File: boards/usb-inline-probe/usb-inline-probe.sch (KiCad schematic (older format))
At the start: 8 parts, among them J1 USB_B, J2 USB_A, J3 SMA, J4 SMA

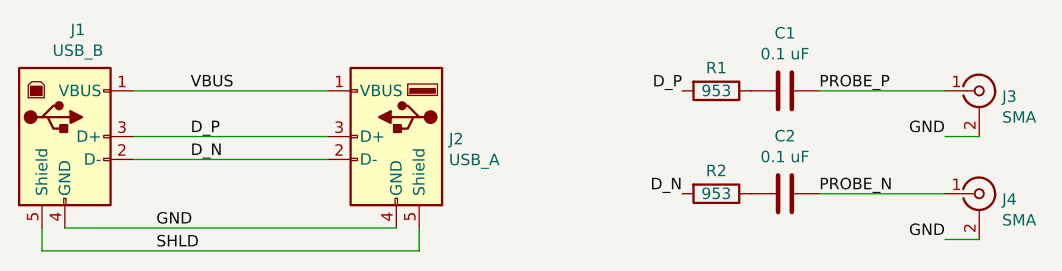
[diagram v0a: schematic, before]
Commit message: Updated coupling cap value
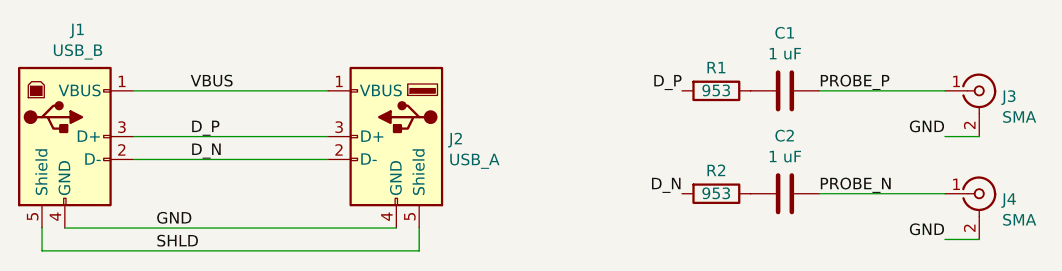
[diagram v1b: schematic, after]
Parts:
- C1, C2: value 0.1 uF -> 1 uF
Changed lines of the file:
@@
 P 8800 2950
 F 0 "C1" V 8548 2950 50  0000 C CNN
-F 1 "0.1 uF" V 8639 2950 50  0000 C CNN
+F 1 "1 uF" V 8639 2950 50  0000 C CNN
 F 2 "azonenberg_pcb:EIA_0402_CAP_NOSILK" H 8838 2800 50  0001 C CNN
 F 3 "" H 8800 2950 50  0001 C CNN
@@
 P 8800 3400
 F 0 "C2" V 8548 3400 50  0000 C CNN
-F 1 "0.1 uF" V 8639 3400 50  0000 C CNN
+F 1 "1 uF" V 8639 3400 50  0000 C CNN
 F 2 "azonenberg_pcb:EIA_0402_CAP_NOSILK" H 8838 3250 50  0001 C CNN
 F 3 "" H 8800 3400 50  0001 C CNN
